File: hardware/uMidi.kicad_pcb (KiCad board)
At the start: 2 copper layers, 66 x 40.6 mm, 61 parts, among them CON1 USB-MINI-B, IC1 ATXMEGA128A4U-M, IC2 74LS14, IC3 LT1129CST-3.3, IC4 6N138, P1 MIDI In, P2 MIDI Thru, P3 MIDI T/O, P4 MIDI Out, P5 5..12 V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

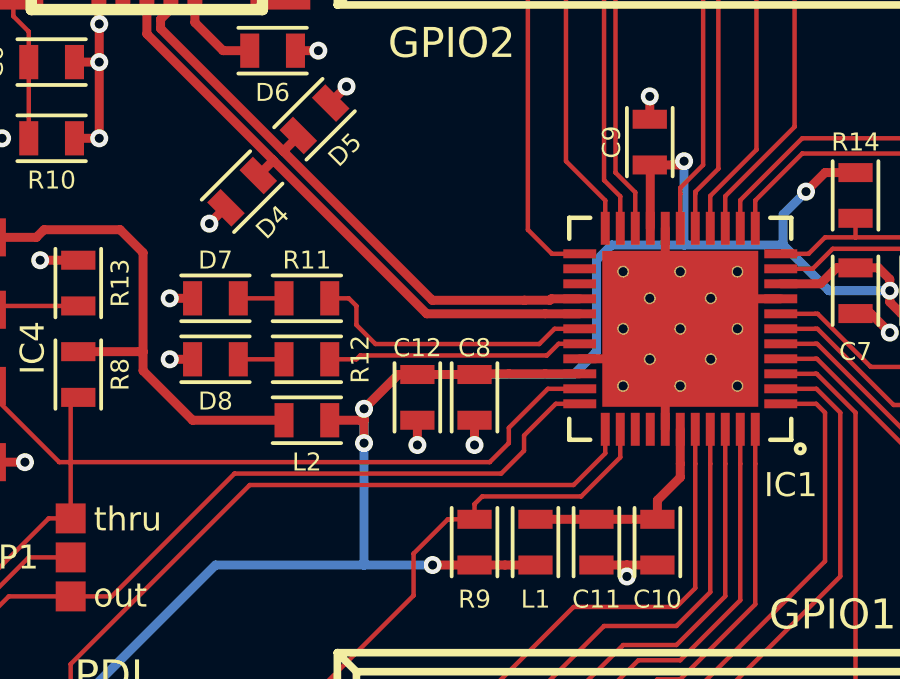
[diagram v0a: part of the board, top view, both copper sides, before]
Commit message: Add solder jumpers to yet unused GPIO pins
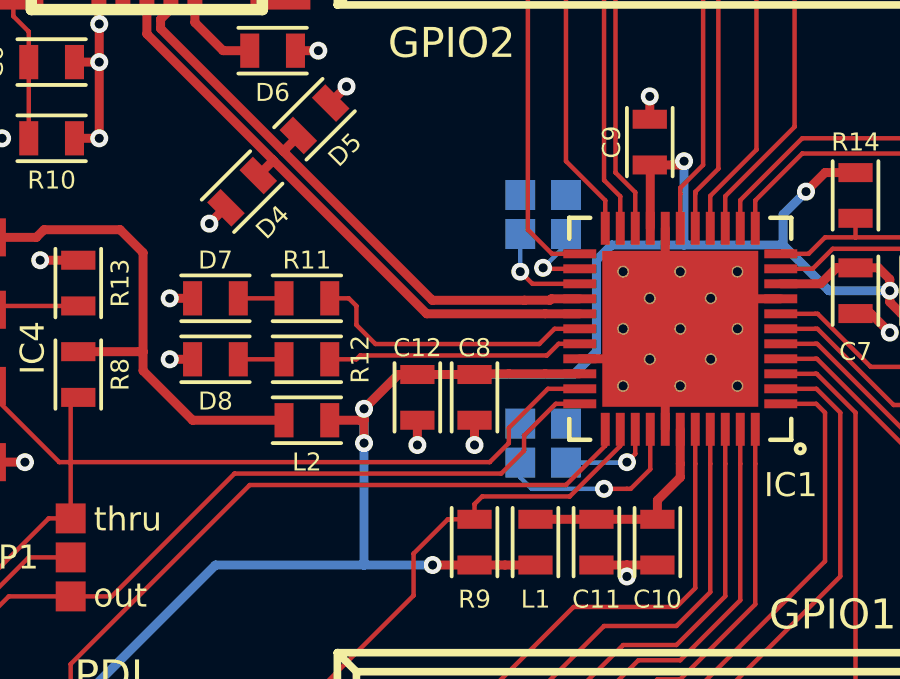
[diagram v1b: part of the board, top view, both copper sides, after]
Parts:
- added JP2: JUMPER, Solderjumper:SJ2, B.Cu at (110.5, 147.3)
- added JP3: JUMPER, Solderjumper:SJ2, B.Cu at (109.0, 147.3)
- added JP4: JUMPER, Solderjumper:SJ2, B.Cu at (110.5, 139.7)
- added JP5: JUMPER, Solderjumper:SJ2, B.Cu at (109.0, 139.7)
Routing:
- net Net-(IC1-Pad37): track 0.00 -> 6.59 mm, vias 0 -> 1
- net Net-(IC1-Pad25): track 0.00 -> 3.41 mm, vias 0 -> 1
- net Net-(IC1-Pad36): track 0.00 -> 3.25 mm, vias 0 -> 1
- net Net-(IC1-Pad24): track 0.00 -> 2.68 mm, vias 0 -> 1

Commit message: Add and use new footprint for USB receptacle
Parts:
- CON1: footprint Connect:USB_MINI_B -> Pinheaders:UX60MB-5ST
- moved CON1 1.27 mm to (96.5, 129.5), turned to 180 degrees
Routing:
- net VBUS: track 28.7 -> 32.0 mm, vias 0 -> 2
